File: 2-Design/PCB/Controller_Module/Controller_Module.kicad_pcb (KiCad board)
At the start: 2 copper layers, 200 x 50 mm, 13 parts, among them J1 Headers_GD1, J2 Headers_GD2, J3 Headers_GD3, J4 Headers_GD4, J5 Headers_GD5, J6 Headers_GD6, J7 Header_I_sense

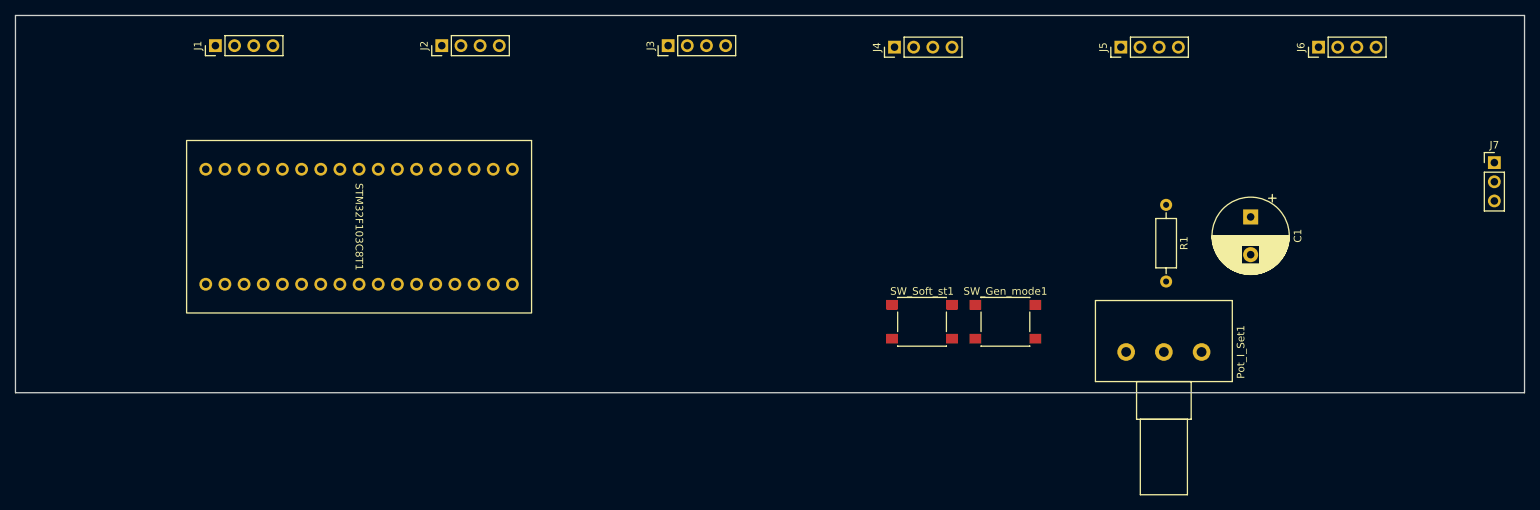
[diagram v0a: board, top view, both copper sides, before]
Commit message: Gate Driver Module minimum load for boost, plus Controller Module advancements
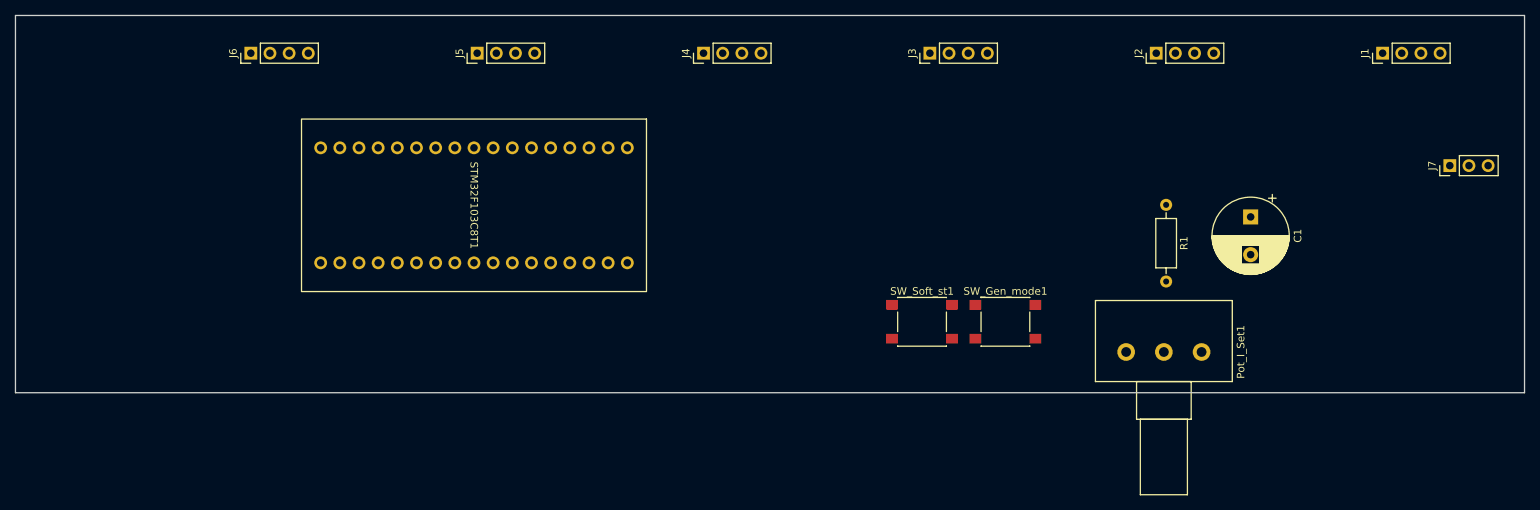
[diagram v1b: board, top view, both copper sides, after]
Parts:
- moved J1 154.7 mm to (241.2, 35.0)
- moved J6 141.5 mm to (91.2, 35.0)
- moved J2 94.7 mm to (211.2, 35.0)
- moved J5 85.3 mm to (121.2, 35.0)
- moved J3 34.7 mm to (181.2, 35.0)
- moved J4 25.3 mm to (151.2, 35.0)
- moved STM32F103C8T1 15.5 mm to (118.2, 55.2)
- moved J7 5.92 mm to (250.1, 49.9), turned to 90 degrees
